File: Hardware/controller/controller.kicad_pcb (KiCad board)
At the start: 4 copper layers, 128.1 x 184.5 mm, 75 parts, among them J101 Conn_02x10_Odd_Even, J102 Conn_02x10_Odd_Even, J103 Conn_02x10_Odd_Even, J301 Conn_ARM_JTAG_SWD_10, J302 Conn_01x03_Male, SW301 B3F-1005, U101 PCA9543A, U201 BD9C301FJ, U302 ATSAME51J20A-A, U303 AT25SF321B-SSHB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

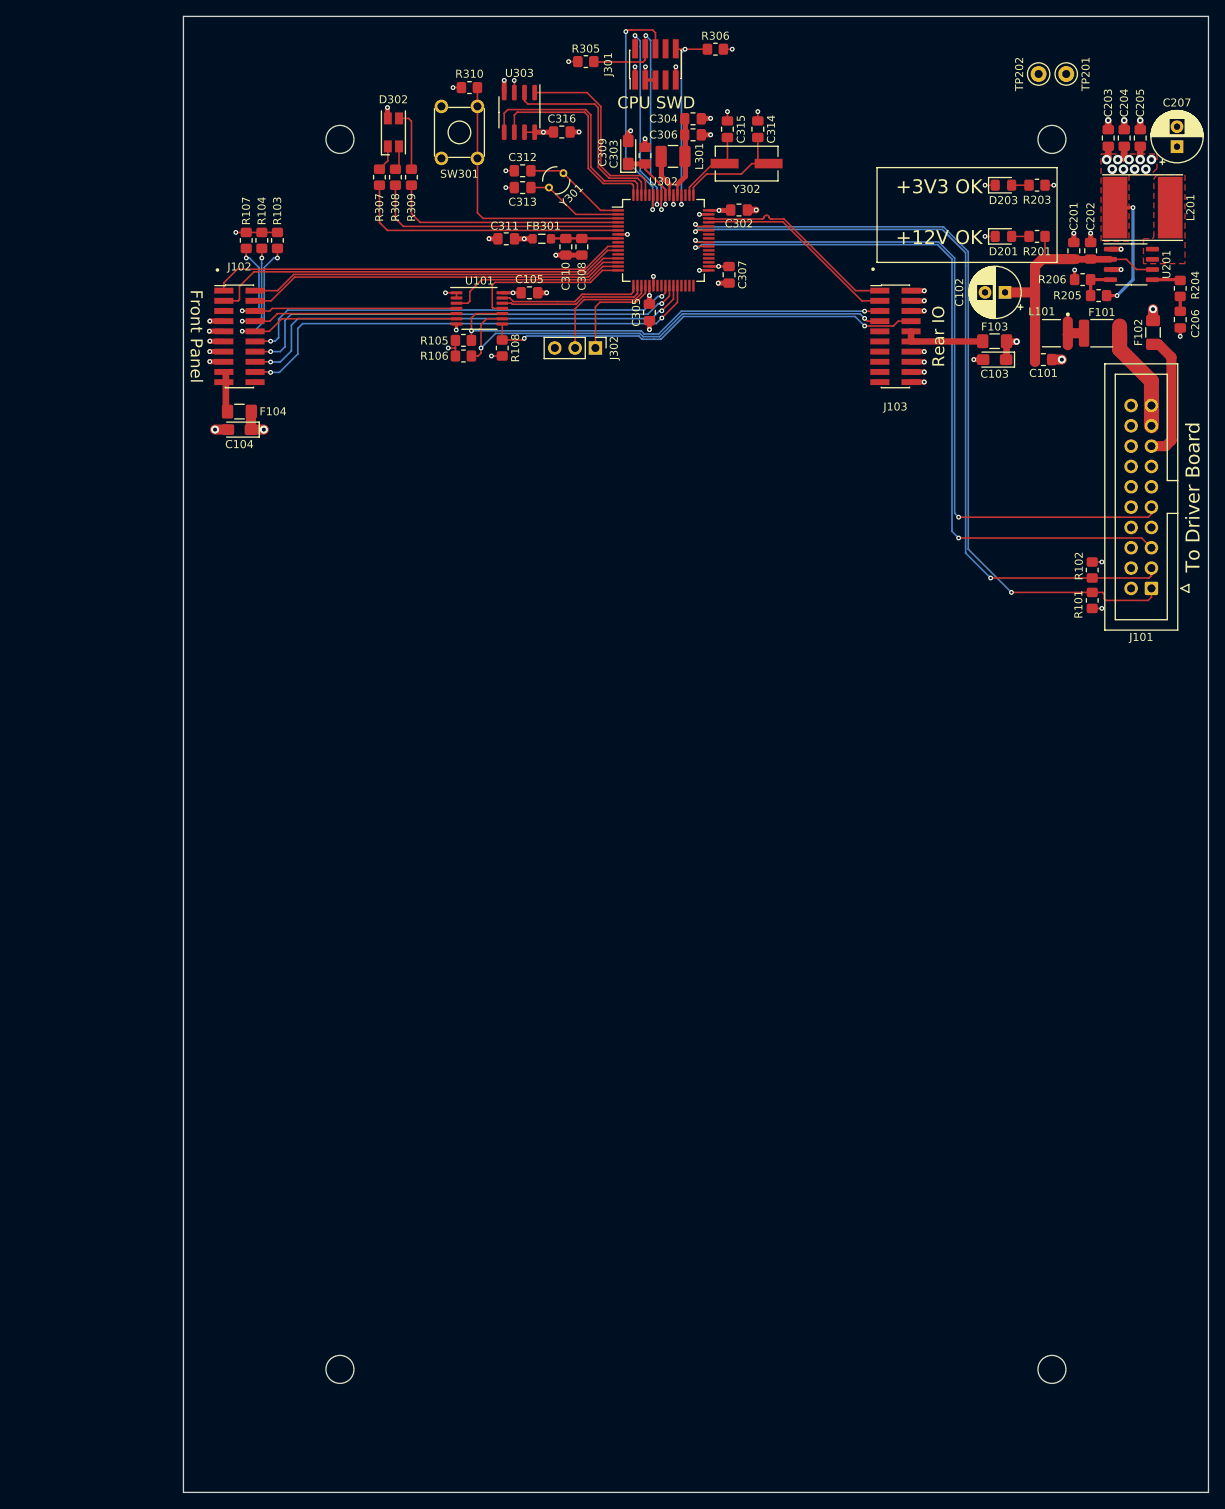
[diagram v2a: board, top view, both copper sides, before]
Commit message: Added Ethernet PHY
- Placed the Ethernet PHY on the controller board, and routed its lines
  to the rear panel connector. The MAC address will be stored in the NOR
  flash, and will need to be programmed in. (This avoids the complexity
  of needing a larger I2C switch to give us another bus for an I2C
  EEPROM; though we could ostensibly put one on the rear IO board.)
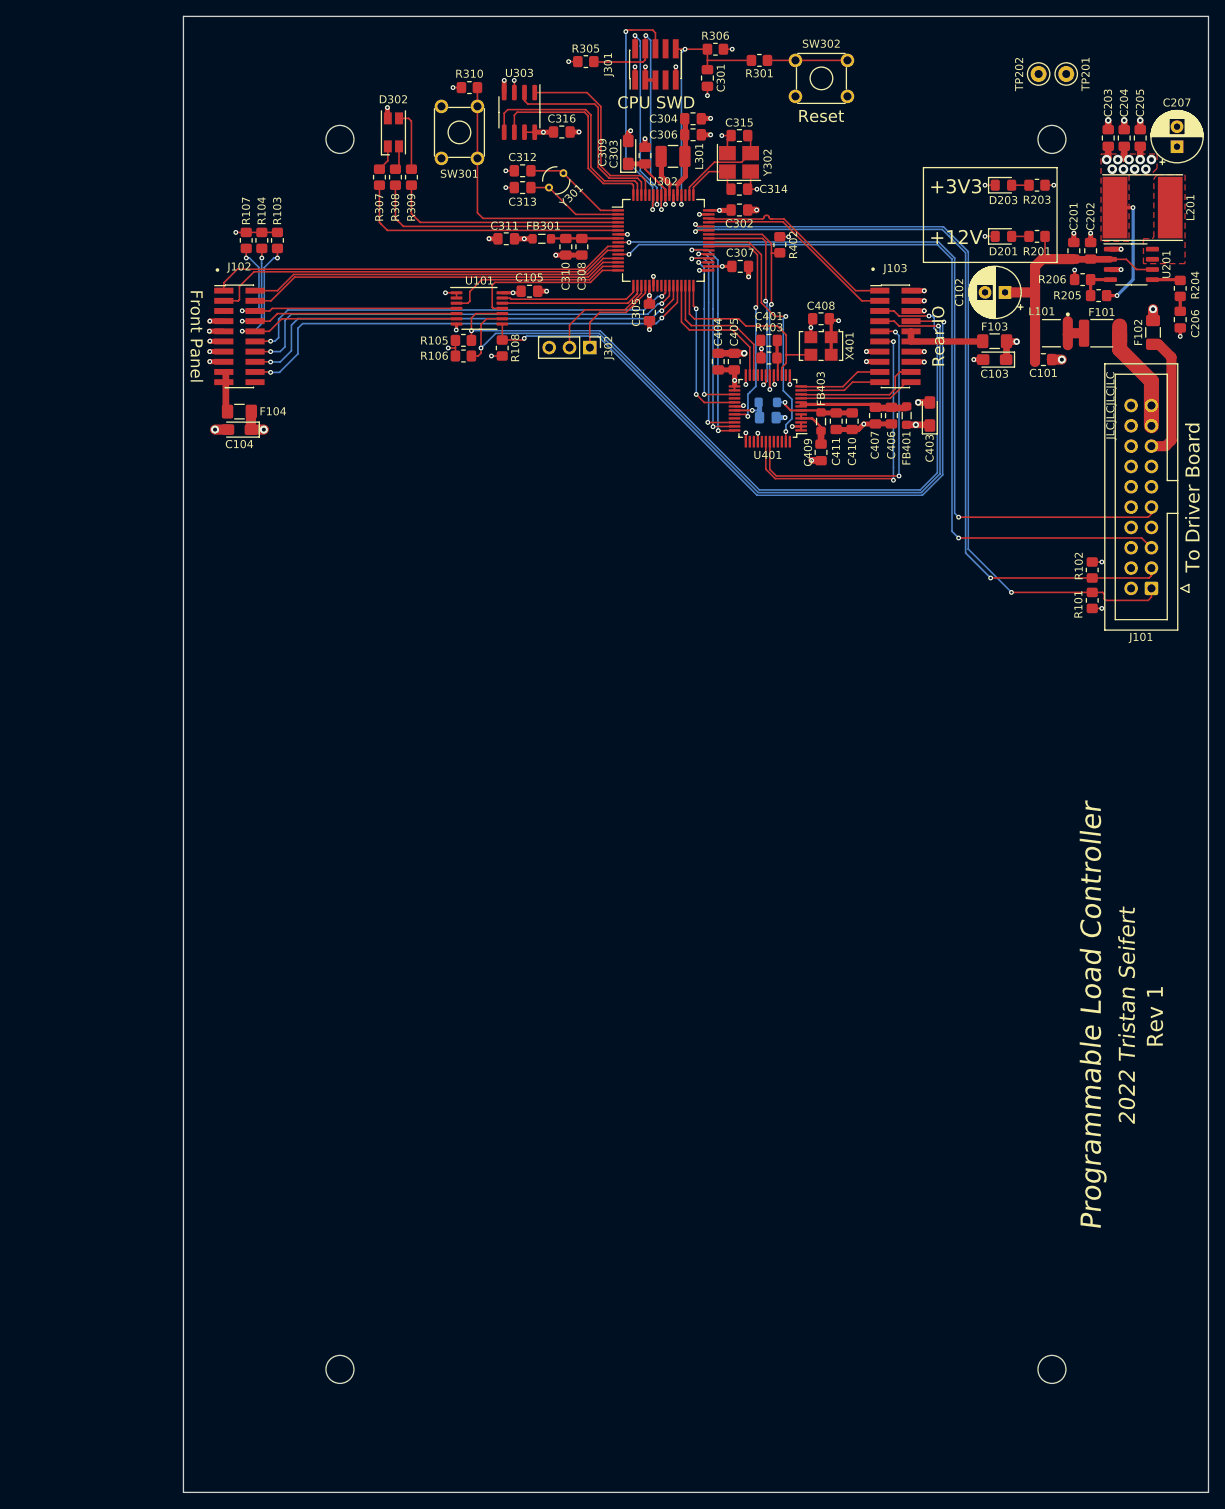
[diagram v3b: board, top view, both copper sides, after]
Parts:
- added C301: 100nF, Capacitor_SMD:C_0805_2012Metric_Pad1.18x1.45mm_HandSolder, F.Cu at (85.5, 27.7)
- added C401: 100pF, Capacitor_SMD:C_0805_2012Metric_Pad1.18x1.45mm_HandSolder, F.Cu at (93.2, 60.5)
- added C403: 10µF, Capacitor_Tantalum_SMD:CP_EIA-3216-18_Kemet-A_Pad1.58x1.35mm_HandSolder, F.Cu at (113.3, 69.7)
- added C404: 22µF, Capacitor_SMD:C_0805_2012Metric_Pad1.18x1.45mm_HandSolder, F.Cu at (86.8, 63.1)
- added C405: 100nF, Capacitor_SMD:C_0805_2012Metric_Pad1.18x1.45mm_HandSolder, F.Cu at (88.8, 63.1)
- added C406: 22µF, Capacitor_SMD:C_0805_2012Metric_Pad1.18x1.45mm_HandSolder, F.Cu at (108.5, 69.9)
- added C407: 100nF, Capacitor_SMD:C_0805_2012Metric_Pad1.18x1.45mm_HandSolder, F.Cu at (106.5, 69.9)
- added C408: 100nF, Capacitor_SMD:C_0805_2012Metric_Pad1.18x1.45mm_HandSolder, F.Cu at (99.7, 57.8)
- added C409: 100nF, Capacitor_SMD:C_0805_2012Metric_Pad1.18x1.45mm_HandSolder, F.Cu at (99.7, 74.5)
- added C410: 1µF, Capacitor_SMD:C_0805_2012Metric_Pad1.18x1.45mm_HandSolder, F.Cu at (103.6, 70.6)
- added C411: 100nF, Capacitor_SMD:C_0805_2012Metric_Pad1.18x1.45mm_HandSolder, F.Cu at (101.6, 70.6)
- added C412: 100nF, Capacitor_SMD:C_0805_2012Metric_Pad1.18x1.45mm_HandSolder, B.Cu at (93.0, 70.2)
- added FB401: FerriteBead_Small, Inductor_SMD:L_0805_2012Metric_Pad1.05x1.20mm_HandSolder, F.Cu at (110.4, 69.9)
- added FB402: FerriteBead_Small, Inductor_SMD:L_0805_2012Metric_Pad1.05x1.20mm_HandSolder, B.Cu at (93.0, 68.2)
- added FB403: FerriteBead_Small, Inductor_SMD:L_0805_2012Metric_Pad1.05x1.20mm_HandSolder, F.Cu at (99.7, 70.7)
- added R301: 330R, Resistor_SMD:R_0805_2012Metric_Pad1.20x1.40mm_HandSolder, F.Cu at (92.0, 25.5)
- added R402: 1k, Resistor_SMD:R_0805_2012Metric_Pad1.20x1.40mm_HandSolder, F.Cu at (94.5, 48.5)
- added R403: 6k49, Resistor_SMD:R_0805_2012Metric_Pad1.20x1.40mm_HandSolder, F.Cu at (93.2, 62.7)
- added SW302: B3F-1002, Button_Switch_THT:SW_TH_Tactile_Omron_B3F-10xx, F.Cu at (96.5, 25.5)
- added U401: KSZ8041TL, Package_QFP:TQFP-48_7x7mm_P0.5mm, F.Cu at (93.0, 69.0)
- added X401: 50MHz, Oscillator:Oscillator_SMD_SeikoEpson_SG8002LB-4Pin_5.0x3.2mm, F.Cu at (99.7, 61.2)
- C312, C313: value 22pF -> 4.7pF
- C314, C315: value 22pF -> 8.2pF
- Y302: footprint Crystal:Crystal_SMD_ECS_CSM3X-2Pin_7.6x4.1mm -> Crystal:Crystal_SMD_3225-4Pin_3.2x2.5mm_HandSoldering
- moved C314 7.85 mm to (89.5, 41.6), turned to 180 degrees
- moved C307 1.75 mm to (89.6, 51.2), turned to 0 degrees
- moved C315 1.70 mm to (89.5, 34.9), turned to 0 degrees
- moved Y302 0.96 mm to (89.5, 38.2), turned to 0 degrees
- moved J302 0.70 mm to (70.8, 61.4)
- moved C105 0.20 mm to (63.2, 54.4)
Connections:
- J103 pad 11: unconnected-(J103-Pad11) -> /ETH_LED0
- J103 pad 13: unconnected-(J103-Pad13) -> GND
- J103 pad 15: unconnected-(J103-Pad15) -> GND
- J103 pad 17: unconnected-(J103-Pad17) -> /ETH_TX-
- J103 pad 18: GND -> /ETH_RX+
- J103 pad 19: unconnected-(J103-Pad19) -> /ETH_TX+
- J103 pad 20: GND -> /ETH_RX-
- J103 pad 9: unconnected-(J103-Pad9) -> /ETH_LED1
- U302 pad 12: unconnected-(U302-Pad12) -> /~{EXT_IRQ}
- U302 pad 31: /CPU/ETH_TXCK -> /CPU/ETH_REFCLK
- U302 pad 39: /~{EXT_IRQ} -> /CPU/~{ETH_IRQ}
- U302 pad 40: /~{EXT_RESET} -> /CPU/~{ETH_RESET}
- U302 pad 9: unconnected-(U302-Pad9) -> /~{EXT_RESET}
- Y302 pad 2: /CPU/XOUT -> GND
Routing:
- net /IO_SCL: track 59.3 -> 100.9 mm
- net /IO_SDA: track 60.2 -> 101.4 mm
- net /ETH_LED1: track 0.00 -> 40.1 mm, vias 0 -> 2
- net /ETH_LED0: track 0.00 -> 39.0 mm, vias 0 -> 2
- net /~{IO_IRQ}: track 55.4 -> 89.9 mm
- net /CPU/~{ETH_RESET}: track 0.00 -> 33.5 mm, vias 0 -> 2
- net GND: track 72.1 -> 104.5 mm, vias 51 -> 65
- net /CPU/ETH_MDIO: track 0.00 -> 29.5 mm, vias 0 -> 2
- net /CPU/ETH_TXD1: track 0.00 -> 29.4 mm, vias 0 -> 2
- net /CPU/~{ETH_IRQ}: track 0.00 -> 29.0 mm, vias 0 -> 2
- net /CPU/ETH_TXEN: track 0.00 -> 27.9 mm, vias 0 -> 2
- net /CPU/ETH_TXD0: track 0.00 -> 26.8 mm, vias 0 -> 2
- net /CPU/ETH_MDC: track 0.00 -> 26.8 mm, vias 0 -> 2
- net /CPU/ETH_REFCLK: track 0.00 -> 25.1 mm
- net /CPU/ETH_CRSDV: track 0.00 -> 21.8 mm, vias 0 -> 2
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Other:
- board text added: "+12V"
- board text added: "+3V3"
- board text added: "2022 Tristan Seifert"
- board text added: "JLCJLCJLCJLC"
- board text added: "Programmable Load Controller"
- board text added: "Reset"
- board text added: "Rev 1"
- board text removed: "+12V OK"
- board text removed: "+3V3 OK"

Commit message: Power button on controller board
- Added a power button (with combination white/amber LED) to the
  controller board; it shall poke through the front panel. It's a soft
  power button, so the micro will actually be awake the entire time.
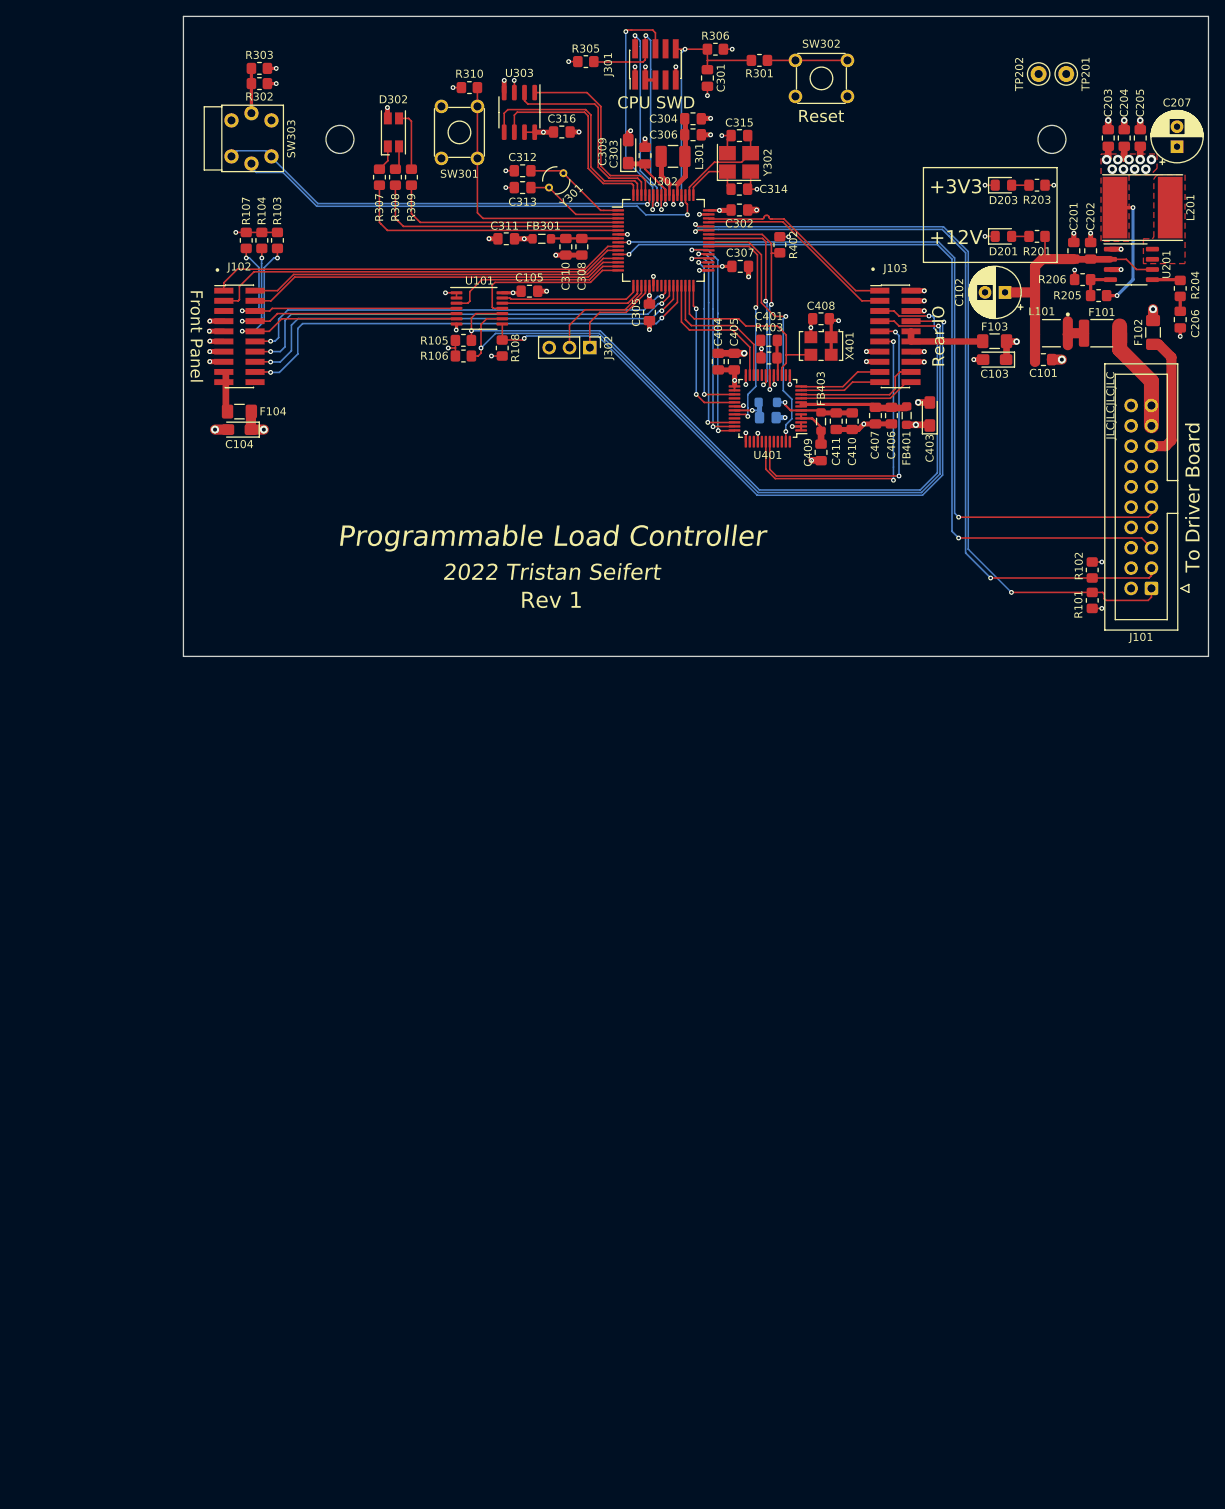
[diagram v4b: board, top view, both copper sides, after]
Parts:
- removed H103, H104: MountingHole, MountingHole:MountingHole_3.5mm
- added R302: 330R, Resistor_SMD:R_0805_2012Metric_Pad1.20x1.40mm_HandSolder, F.Cu at (29.5, 28.4)
- added R303: 330R, Resistor_SMD:R_0805_2012Metric_Pad1.20x1.40mm_HandSolder, F.Cu at (29.5, 26.5)
- added SW303: 228ADS2AAWFCMBA, programmable-load:CTS-228ADS2, F.Cu at (26.0, 33.0)
- moved C309 0.10 mm to (75.6, 36.9)
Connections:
- U302 pad 23: unconnected-(U302-Pad23) -> /CPU/BEEPER
- U302 pad 51: unconnected-(U302-Pad51) -> /CPU/PWRLED
- U302 pad 60: unconnected-(U302-Pad60) -> /CPU/PWRBTN
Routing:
- net /CPU/PWRLED: track 0.00 -> 60.0 mm, vias 0 -> 1
- net /CPU/PWRBTN: track 0.00 -> 56.4 mm, vias 0 -> 1
- net Net-(R302-Pad2): track 0.00 -> 5.60 mm
- net GND: track 104.5 -> 105.6 mm, vias 65 -> 66
- net +3V3: track 89.5 -> 90.6 mm, vias 38 -> 39
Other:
- board size 128.1 x 184.5 mm -> 128.1 x 80 mm
- board text removed: "Heat Sink Area"

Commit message: Added beeper to control board
- Added a beeper (magnetic transducer, including an amplifier to go with
  it) to the controller board so we can make loud annoying beeping
  noises as desired

- A few minor tweaks to the layout of the control board
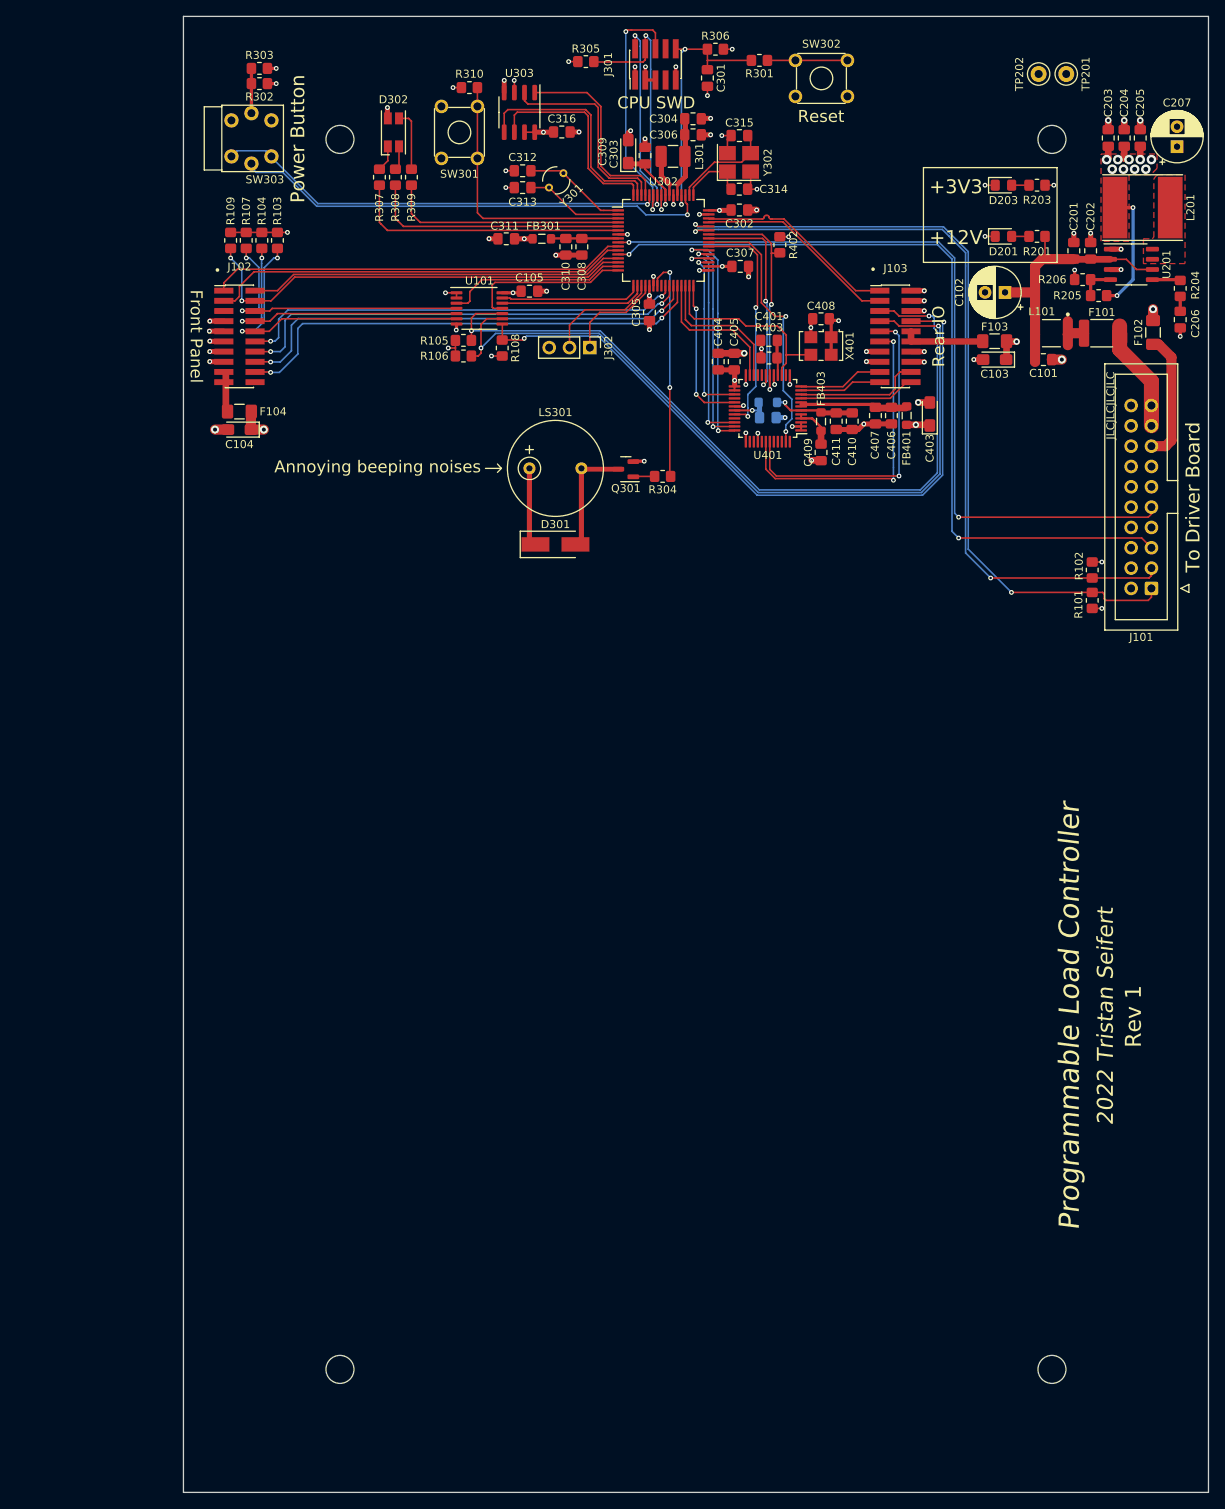
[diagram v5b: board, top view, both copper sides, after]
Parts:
- added D301: SM4007, Diode_SMD:D_SMA_Handsoldering, F.Cu at (66.5, 86.0)
- added H103: MountingHole, MountingHole:MountingHole_3.5mm, F.Cu at (128.6, 189.1)
- added H104: MountingHole, MountingHole:MountingHole_3.5mm, F.Cu at (39.6, 189.1)
- added LS301: Speaker, programmable-load:PUI-AT-1224-TWT, F.Cu at (66.5, 76.5)
- added Q301: MMBT3904, Package_TO_SOT_SMD:SOT-23, F.Cu at (75.3, 76.6)
- added R109: 10k, Resistor_SMD:R_0805_2012Metric_Pad1.20x1.40mm_HandSolder, F.Cu at (25.9, 48.0)
- added R304: 330R, Resistor_SMD:R_0805_2012Metric_Pad1.20x1.40mm_HandSolder, F.Cu at (79.9, 77.5)
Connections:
- net /~{DISP_RESET} renamed /~{FRONT_RESET}
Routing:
- net /CPU/BEEPER: track 0.00 -> 28.8 mm, vias 0 -> 2
- net Net-(D301-Pad2): track 0.00 -> 14.9 mm
- net +3V3: track 90.6 -> 102.3 mm
- net /~{FRONT_RESET}: track 47.4 -> 56.2 mm, vias 0 -> 2
- net Net-(Q301-Pad1): track 0.00 -> 2.16 mm
- net GND: track 105.6 -> 106.9 mm, vias 66 -> 67
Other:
- board size 128.1 x 80 mm -> 128.1 x 184.5 mm
- board text added: "Annoying beeping noises"
- board text added: "Power Button"
